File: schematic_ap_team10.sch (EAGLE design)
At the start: 47 parts, among them J1 FTDI_DEVICE, M1 WIRELESS-NRF24L01, U1 ATMEGA328P_TQFP, U2 GY-521MPU6050

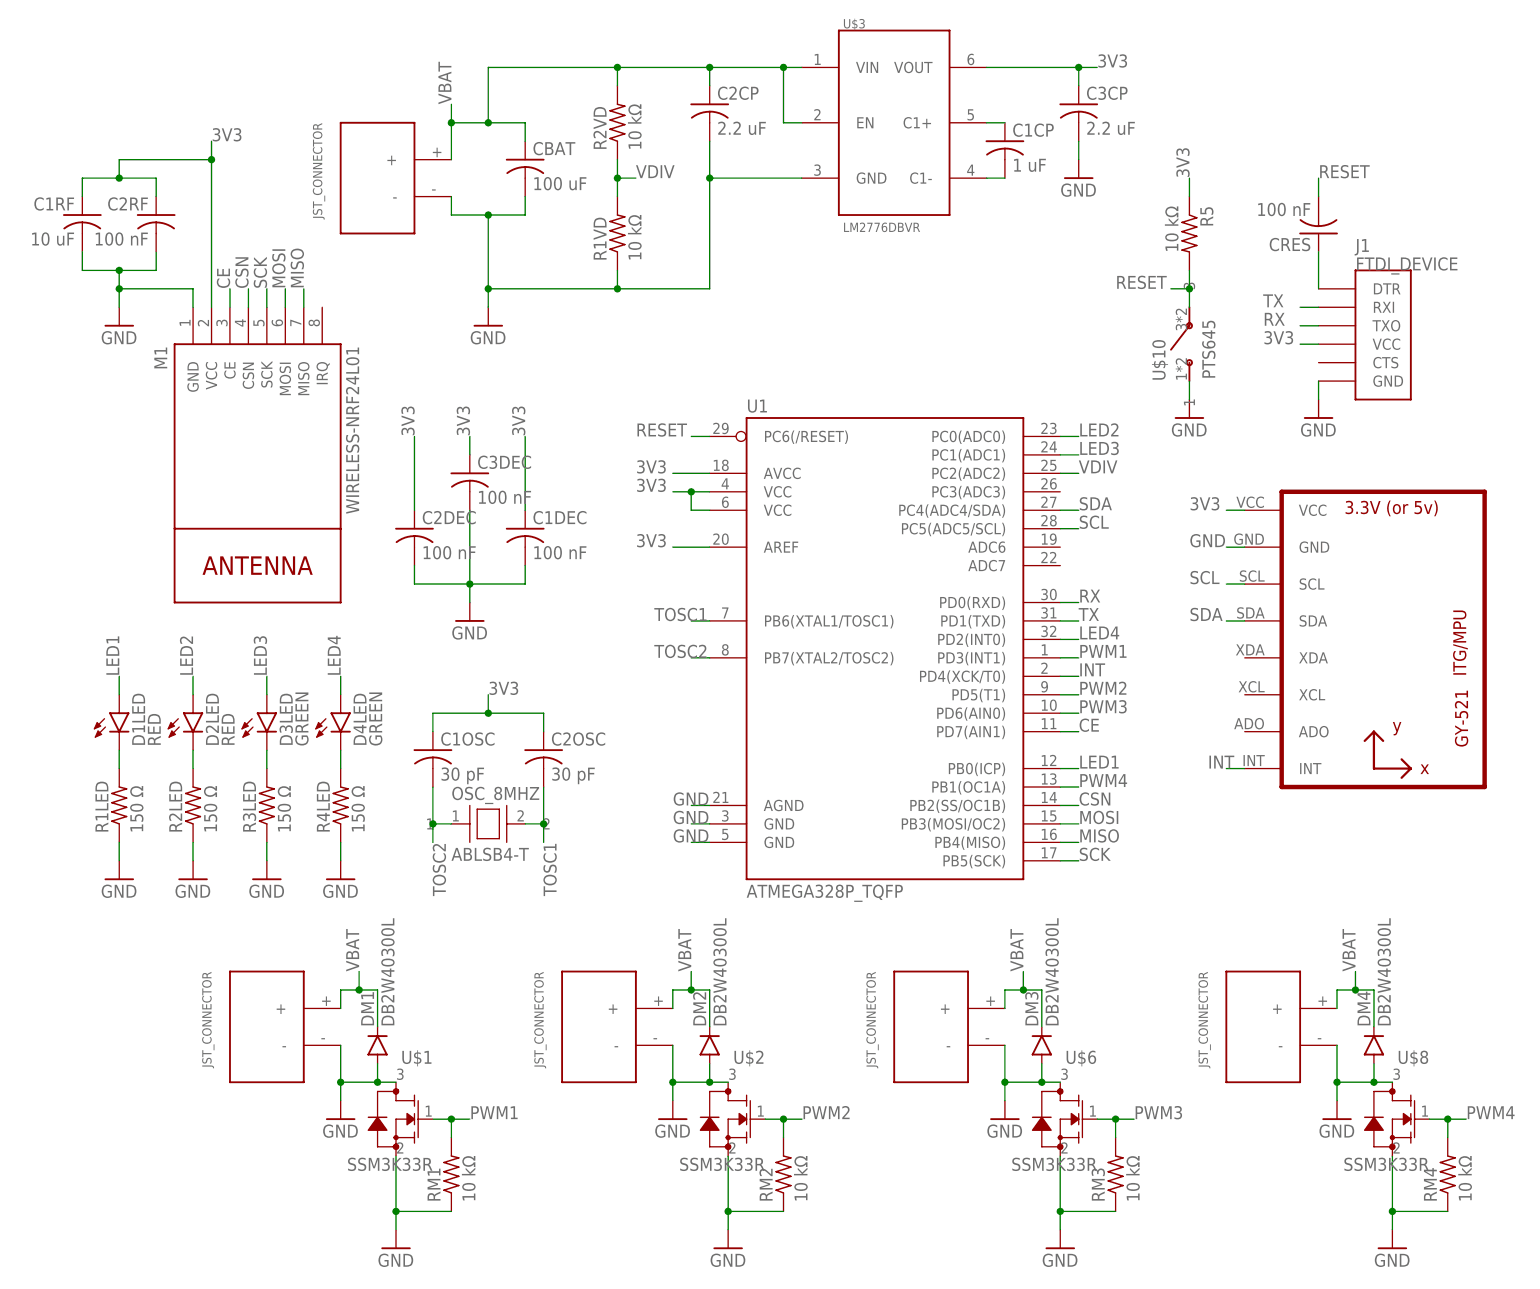
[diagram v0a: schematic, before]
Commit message: 5th Draft
Changed the layout to have JSTs on the side
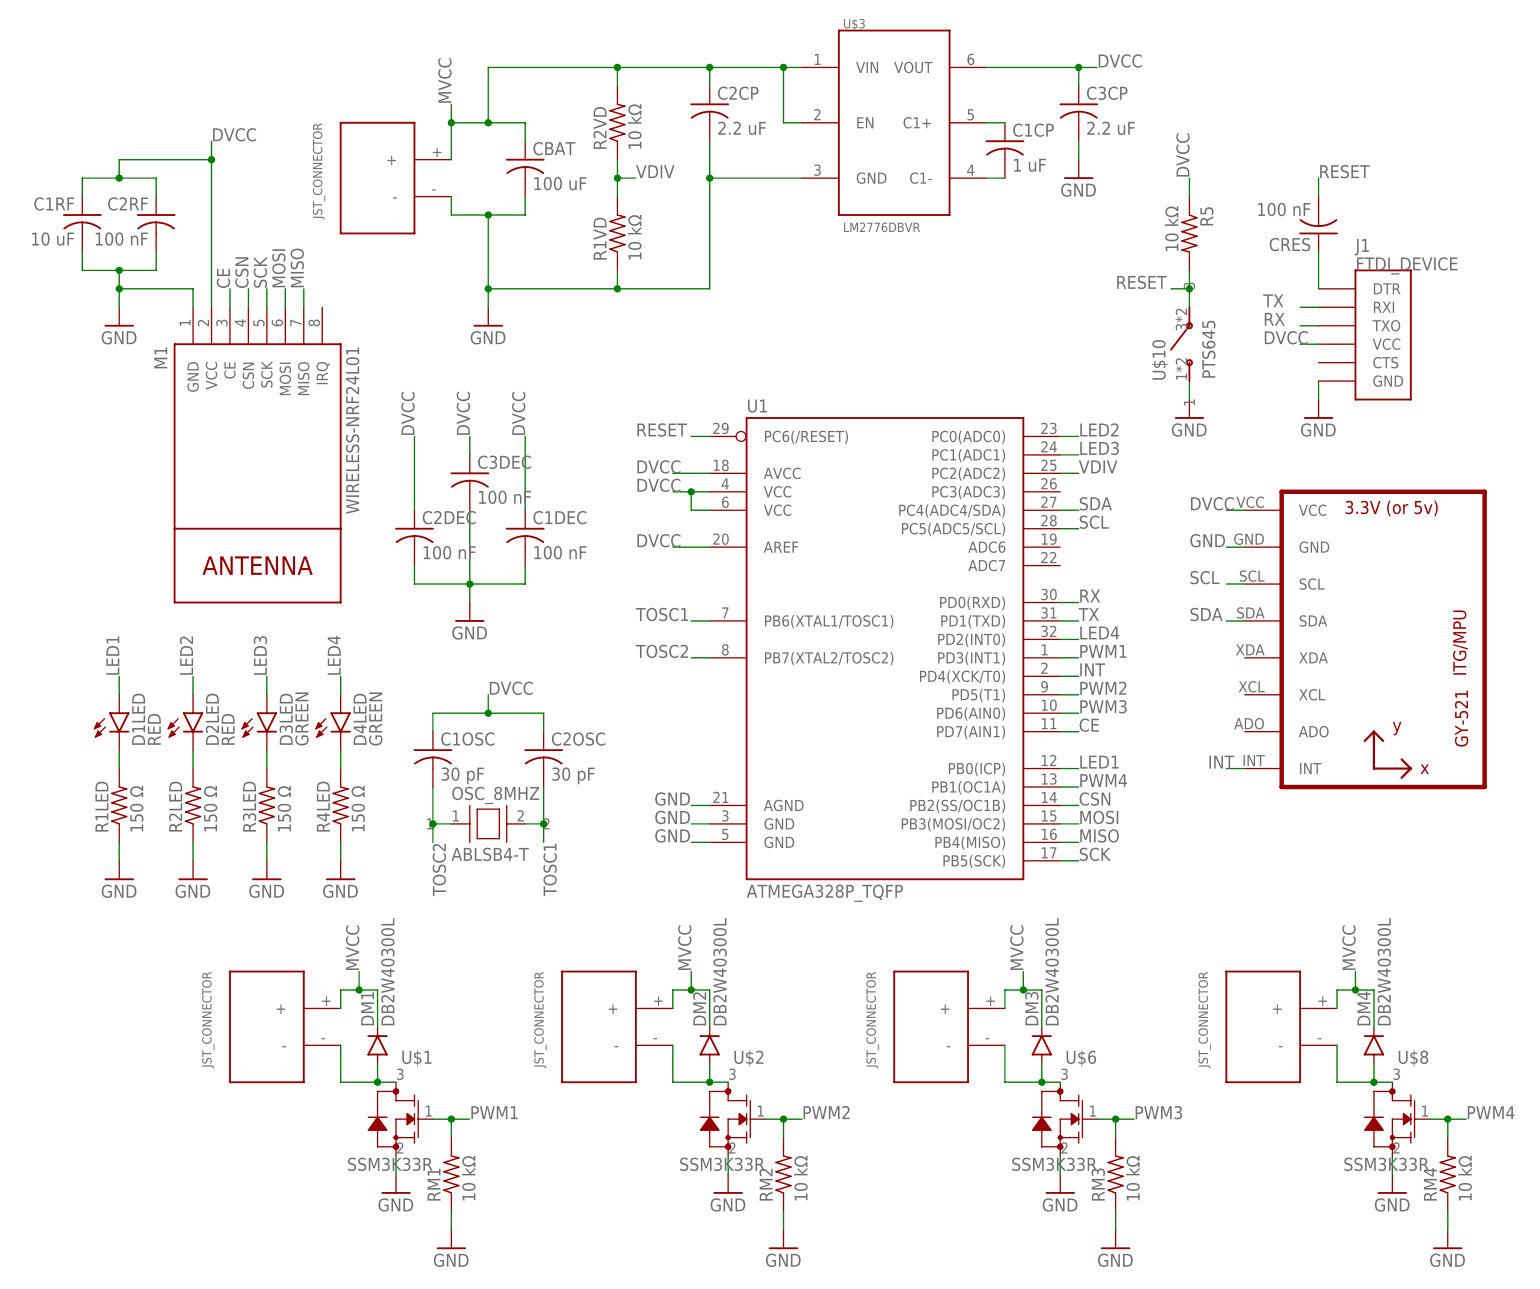
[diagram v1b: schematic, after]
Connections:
- net 3V3 renamed DVCC
- net VBAT renamed MVCC
- new net N$1: DM1.PPIN, U$1.3, U$4.-
- new net N$2: DM2.PPIN, U$2.3, U$5.-
- new net N$4: DM3.PPIN, U$6.3, U$7.-
- new net N$5: DM4.PPIN, U$8.3, U$9.-
- net GND: no longer DM1.PPIN, DM2.PPIN, DM3.PPIN, DM4.PPIN, U$1.3, U$2.3, U$4.-, U$5.-, U$6.3, U$7.-, U$8.3, U$9.-

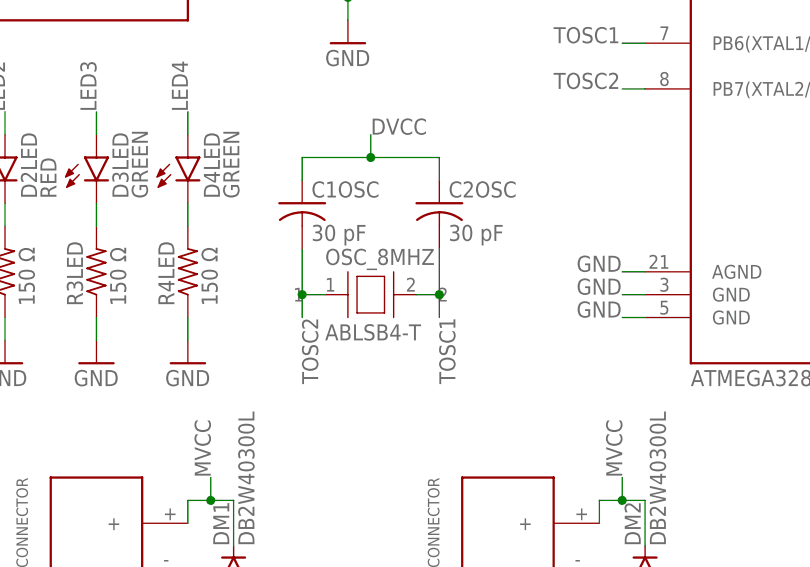
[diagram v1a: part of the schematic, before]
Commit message: Actual 5th (final?) Draft
Changed some parts as well (the oscillator) and moved stuff around.
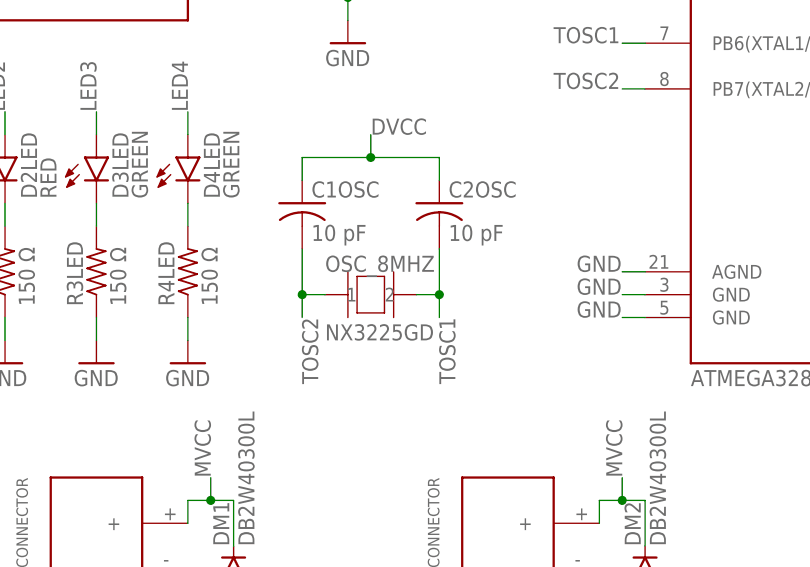
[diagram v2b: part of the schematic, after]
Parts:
- C1OSC, C2OSC: value 30 pF -> 10 pF
- OSC_8MHZ: value ABLSB4-T -> NX3225GD; device ABLS_B4_T:ABLSB4-T -> NX3225GD:NX3225GD
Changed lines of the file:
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@@
 <part name="C3DEC" library="rcl" deviceset="C-US" device="C0603" value="100 nF"/>
 <part name="GND1" library="supply1" deviceset="GND" device=""/>
-<part name="C2OSC" library="rcl" deviceset="C-US" device="C0603" value="30 pF"/>
-<part name="C1OSC" library="rcl" deviceset="C-US" device="C0603" value="30 pF"/>
+<part name="C2OSC" library="rcl" deviceset="C-US" device="C0603" value="10 pF"/>
+<part name="C1OSC" library="rcl" deviceset="C-US" device="C0603" value="10 pF"/>
 <part name="U$3" library="LM2776" deviceset="LM2776" device="DBVR"/>
 <part name="C1CP" library="rcl" deviceset="C-US" device="C0603" value="1 uF"/>
@@
 <part name="C3CP" library="rcl" deviceset="C-US" device="C0603" value="2.2 uF"/>
 <part name="GND3" library="supply1" deviceset="GND" device=""/>
-<part name="OSC_8MHZ" library="ABLS_B4_T" deviceset="ABLS" device="B4-T"/>
 <part name="GND6" library="supply1" deviceset="GND" device=""/>
 <part name="U$4" library="quad" deviceset="JST_CONNECTOR_FEMALE" device=""/>
@@
 <part name="GND17" library="supply1" deviceset="GND" device=""/>
 <part name="GND18" library="supply1" deviceset="GND" device=""/>
+<part name="OSC_8MHZ" library="NX3225GD" deviceset="NX3225GD" device=""/>
 </parts>
 <sheets>
@@
 <instance part="C3CP" gate="G$1" x="25.4" y="76.2"/>
 <instance part="GND3" gate="1" x="25.4" y="66.04"/>
-<instance part="OSC_8MHZ" gate="G$1" x="-55.88" y="-22.86"/>
 <instance part="GND6" gate="1" x="-68.58" y="-73.66"/>
 <instance part="U$4" gate="G$1" x="-86.36" y="-50.8" rot="MR270"/>
@@
 <instance part="GND17" gate="1" x="30.48" y="-81.28"/>
 <instance part="GND18" gate="1" x="76.2" y="-81.28"/>
+<instance part="OSC_8MHZ" gate="G$1" x="-55.88" y="-22.86"/>
 </instances>
 <busses>
@@
 <segment>
 <pinref part="C2OSC" gate="G$1" pin="2"/>
+<wire x1="-48.26" y1="-25.4" x2="-48.26" y2="-22.86" width="0.1524" layer="91"/>
+<label x="-48.26" y="-25.4" size="1.778" layer="95" rot="R270"/>
+<pinref part="OSC_8MHZ" gate="G$1" pin="2"/>
 <wire x1="-48.26" y1="-22.86" x2="-48.26" y2="-17.78" width="0.1524" layer="91"/>
-<wire x1="-48.26" y1="-22.86" x2="-48.26" y2="-25.4" width="0.1524" layer="91"/>
-<pinref part="OSC_8MHZ" gate="G$1" pin="2"/>
 <wire x1="-50.8" y1="-22.86" x2="-48.26" y2="-22.86" width="0.1524" layer="91"/>
 <junction x="-48.26" y="-22.86"/>
-<label x="-48.26" y="-25.4" size="1.778" layer="95" rot="R270"/>
 </segment>
 </net>
@@
 <pinref part="C1OSC" gate="G$1" pin="2"/>
 <wire x1="-63.5" y1="-25.4" x2="-63.5" y2="-22.86" width="0.1524" layer="91"/>
+<label x="-63.5" y="-25.4" size="1.778" layer="95" rot="R270"/>
+<pinref part="OSC_8MHZ" gate="G$1" pin="1"/>
 <wire x1="-63.5" y1="-22.86" x2="-63.5" y2="-17.78" width="0.1524" layer="91"/>
-<pinref part="OSC_8MHZ" gate="G$1" pin="1"/>
 <wire x1="-60.96" y1="-22.86" x2="-63.5" y2="-22.86" width="0.1524" layer="91"/>
 <junction x="-63.5" y="-22.86"/>
-<label x="-63.5" y="-25.4" size="1.778" layer="95" rot="R270"/>
-</segment>
-</net>
+</segment>
+</net>

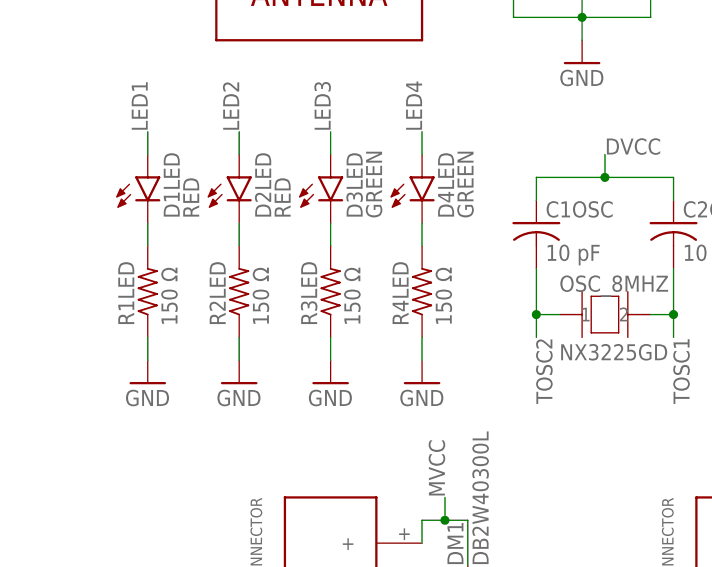
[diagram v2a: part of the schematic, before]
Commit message: LED Resistor Update
150Ohm -> 65Ohm
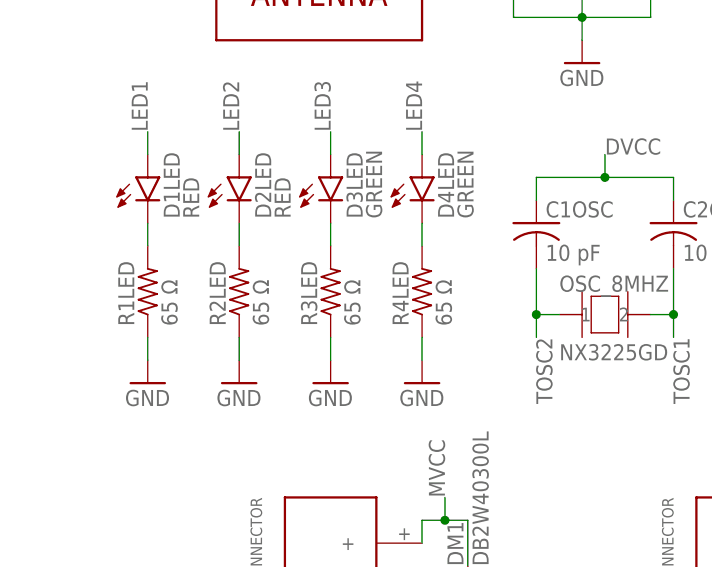
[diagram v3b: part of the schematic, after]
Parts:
- R1LED, R2LED, R3LED, R4LED: value 150 Ω -> 65 Ω
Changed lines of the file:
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@@
 <part name="D3LED" library="LEDs" deviceset="LED-GREEN" device="0603" value="GREEN"/>
 <part name="D4LED" library="LEDs" deviceset="LED-GREEN" device="0603" value="GREEN"/>
-<part name="R4LED" library="resistor" deviceset="R-US_" device="R0603" value="150 Ω"/>
+<part name="R4LED" library="resistor" deviceset="R-US_" device="R0603" value="65 Ω"/>
 <part name="GND7" library="supply1" deviceset="GND" device=""/>
-<part name="R2LED" library="resistor" deviceset="R-US_" device="R0603" value="150 Ω"/>
+<part name="R2LED" library="resistor" deviceset="R-US_" device="R0603" value="65 Ω"/>
 <part name="GND8" library="supply1" deviceset="GND" device=""/>
-<part name="R3LED" library="resistor" deviceset="R-US_" device="R0603" value="150 Ω"/>
+<part name="R3LED" library="resistor" deviceset="R-US_" device="R0603" value="65 Ω"/>
 <part name="GND9" library="supply1" deviceset="GND" device=""/>
-<part name="R1LED" library="resistor" deviceset="R-US_" device="R0603" value="150 Ω"/>
+<part name="R1LED" library="resistor" deviceset="R-US_" device="R0603" value="65 Ω"/>
 <part name="GND10" library="supply1" deviceset="GND" device=""/>
 <part name="J1" library="quad" deviceset="FTDI_DEVICE" device=""/>
